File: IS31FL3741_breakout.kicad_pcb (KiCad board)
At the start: 2 copper layers, 42.5 x 44 mm, 60 parts, among them J1 CONN_PMOD, J2 Conn_02x08_Odd_Even, J3 Conn_02x08_Odd_Even, J4 Conn_02x08_Odd_Even, U1 IS31FL3741

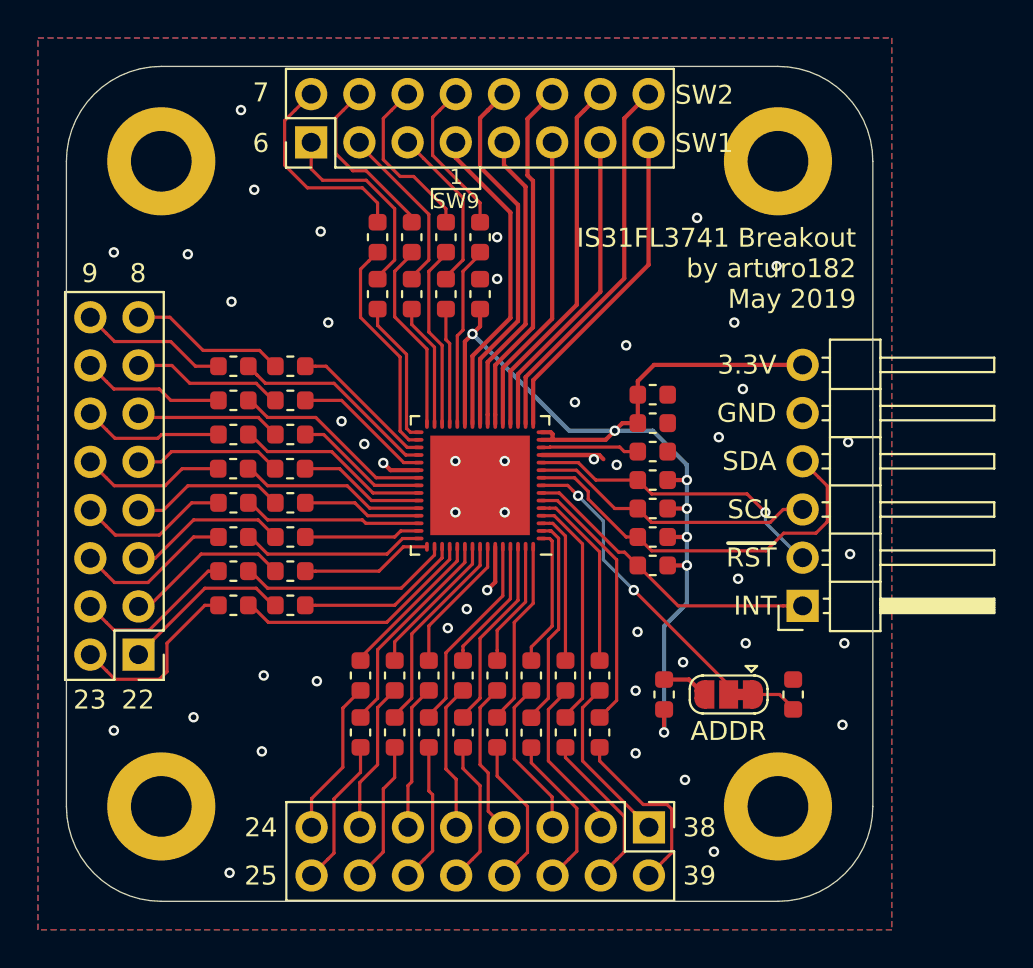
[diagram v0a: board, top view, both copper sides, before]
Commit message: Fix the QFN pin length
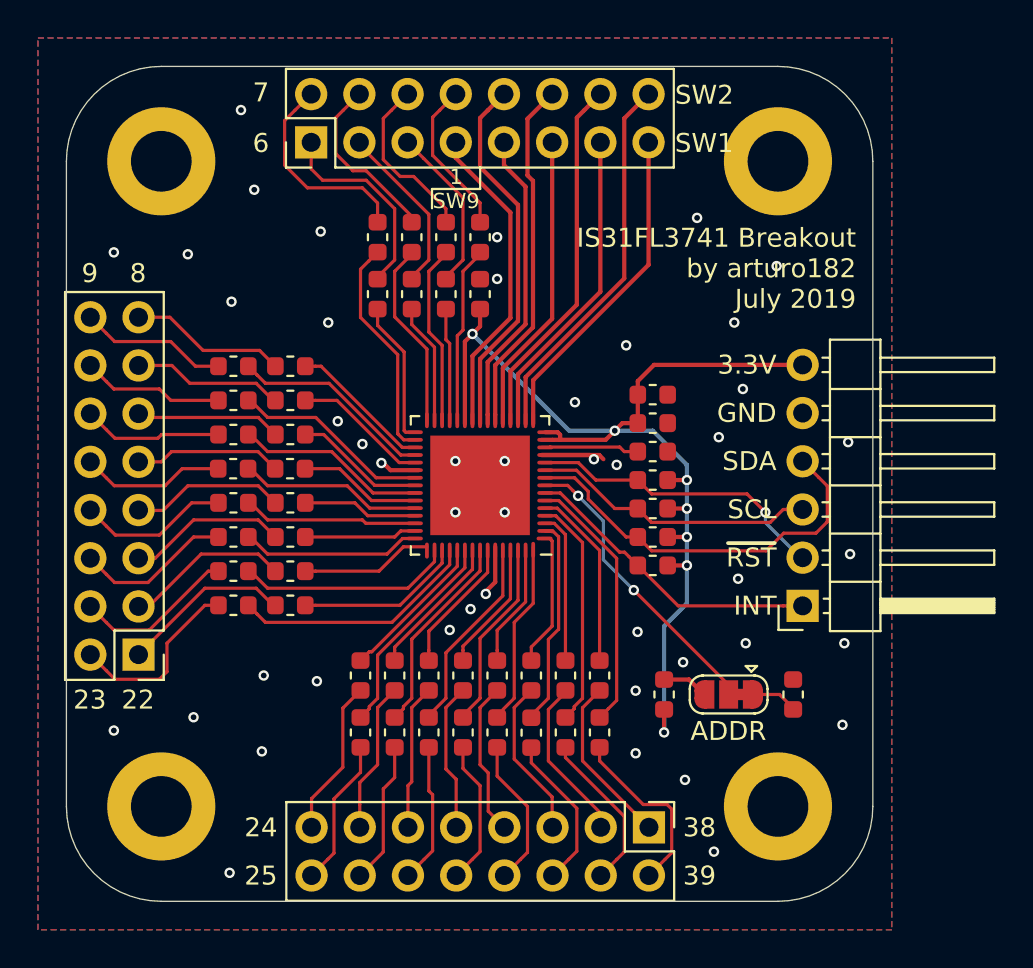
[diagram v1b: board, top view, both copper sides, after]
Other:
- board text added: "IS31FL3741 Breakout by arturo182 July 2019"
- board text added: "JLCJLCJLCJLC"
